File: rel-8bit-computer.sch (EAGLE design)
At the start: 199 parts, among them IC1 74LS04N, IC12 74LS139N, IC2 74LS04N, IC3 74LS04N, IC35 74LS32N, IC37 74LS08N, IC38 74LS08N, IC39 74LS32N, IC4 74LS04N, IC41 74LS08N, IC42 74LS32N, IC44 74LS08N, IC45 74LS32N, IC46 74LS86N, IC47 74LS86N, IC48 74LS32N, IC5 74LS04N, IC50 74LS08N, IC51 74LS08N, IC52 74LS32N, IC54 74LS08N, IC55 74LS32N, IC57 74LS08N, IC58 74LS32N, IC6 74LS04N, IC7 74LS04N, IC8 74LS04N, Q1 BC556, Q2 BS170

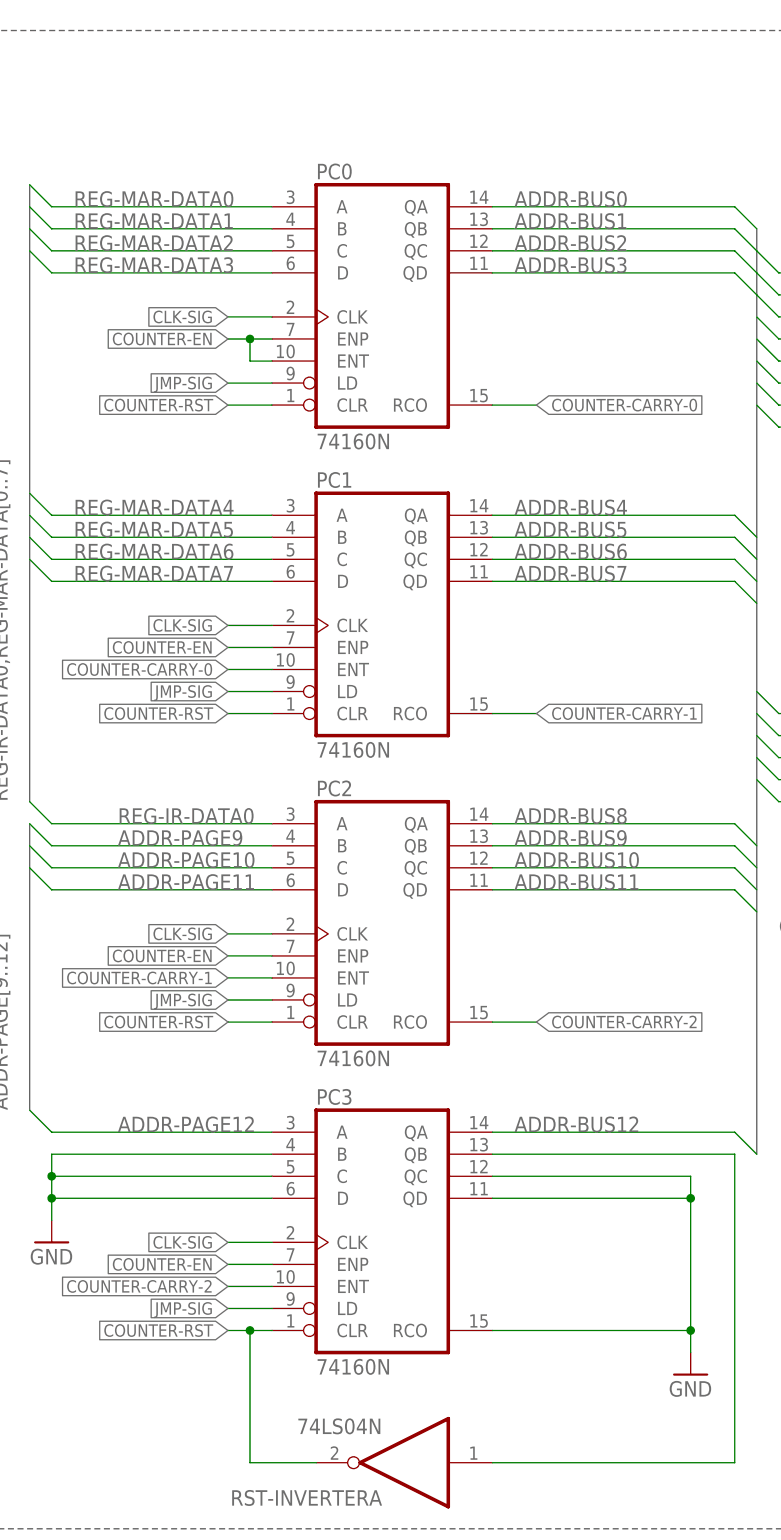
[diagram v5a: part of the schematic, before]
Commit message: Added initial description for PC (program counter) design
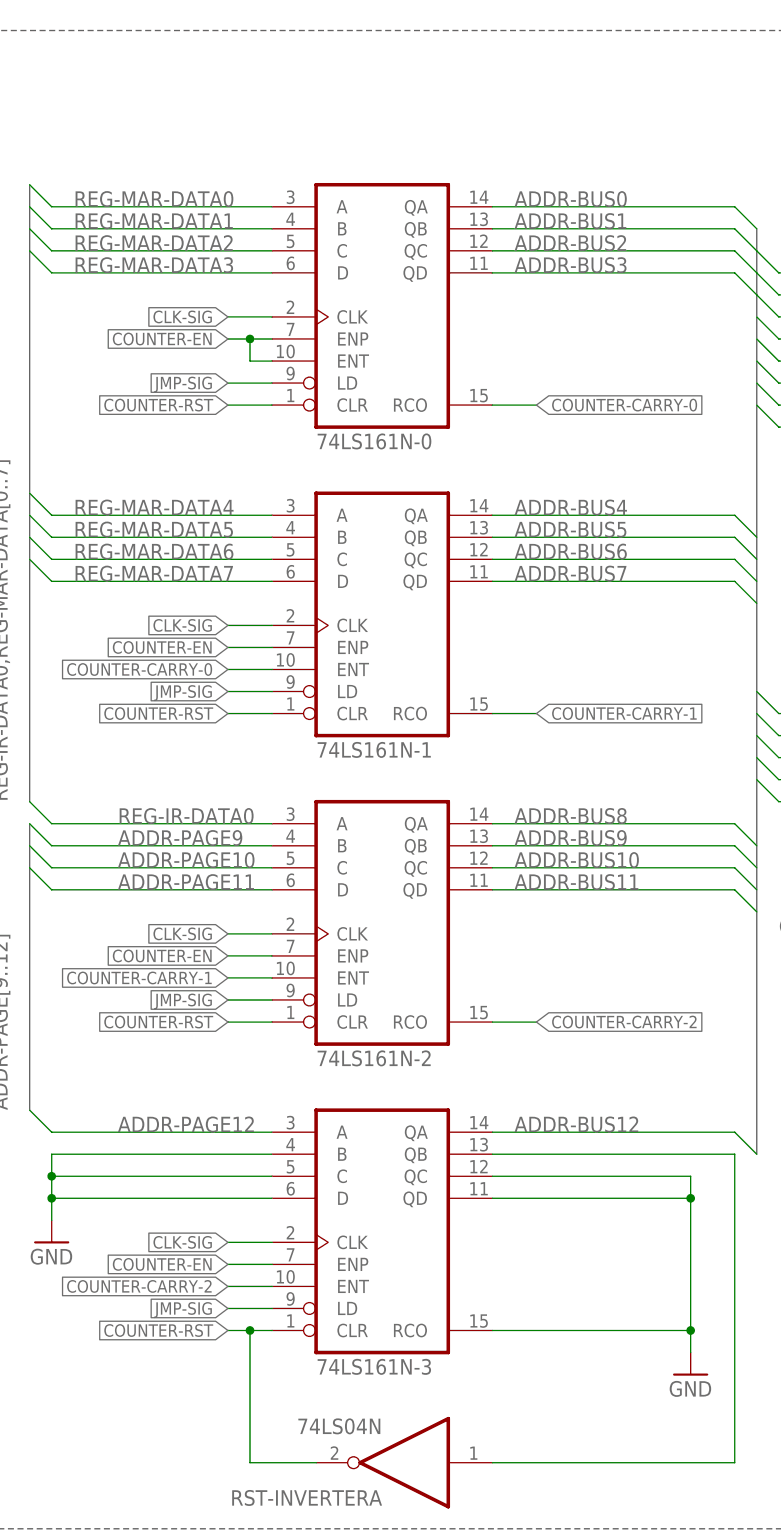
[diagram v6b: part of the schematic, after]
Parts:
- renumbered PC0 to 74LS161N-0, PC1 to 74LS161N-1, PC2 to 74LS161N-2, PC3 to 74LS161N-3

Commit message: Fixed PCH in/out added CS (chip select) reg
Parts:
- added CHIP-SELECT-REG-0: 74LS173N, 74xx-eu:74LS173N
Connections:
- net COUNTER0-OUT renamed PCL-OUT
- net COUNTER1-OUT renamed PCH-OUT
- net MEM-EN-A0 renamed CEN-A0
- net MEM-EN-A1 renamed CEN-A1
- net MEM-EN-A2 renamed CEN-A2
- net MEM-EN-A3 renamed CEN-A3
- net MEM-EN-B0 renamed CEN-B0
- net MEM-EN-B1 renamed CEN-B1
- net MEM-EN-B2 renamed CEN-B2
- net MEM-EN-B3 renamed CEN-B3
- removed net ADDR-BUS10: 74LS161N-2A.QC, ADDR-R/P-SW-2A.3A, PC-BUF-HA.A3
- removed net ADDR-BUS11: 74LS161N-2A.QD, ADDR-R/P-SW-2A.4A, PC-BUF-HA.A4
- removed net ADDR-BUS8: 74LS161N-2A.QA, ADDR-R/P-SW-2A.1A, PC-BUF-HA.A1
- removed net ADDR-BUS9: 74LS161N-2A.QB, ADDR-R/P-SW-2A.2A, PC-BUF-HA.A2
- removed net ADDR-PAGE12: 74LS161N-3A.A, PAGE-ADDR-REG-0A.Q4
- removed net JMP-SIG: 74LS161N-0A.LD, 74LS161N-1A.LD, 74LS161N-2A.LD, 74LS161N-3A.LD
- new net ADDR-EX: 74LS161N-3A.QA
- new net ADDR-PAGE8: ADDR-R/P-SW-2A.1A
- new net CS-EN: CHIP-SELECT-REG-0A.G1, CHIP-SELECT-REG-0A.G2
- new net CS0: CHIP-SELECT-REG-0A.Q1, DEMUX-2X4-0A.A
- new net CS1: CHIP-SELECT-REG-0A.Q2, DEMUX-2X4-0A.B
- new net PCH-IN: 74LS161N-2A.LD, 74LS161N-3A.LD
- new net PCL-IN: 74LS161N-0A.LD, 74LS161N-1A.LD
- net ADDR-BUS12: now also 74LS161N-3A.A, CHIP-SELECT-REG-0A.Q3; no longer 74LS161N-3A.QA, PC-BUF-HA.A5
- net ADDR-BUS4: now also 74LS161N-2A.QA, PC-BUF-HA.A1
- net ADDR-BUS5: now also 74LS161N-2A.QB, PC-BUF-HA.A2
- net ADDR-BUS6: now also 74LS161N-2A.QC, PC-BUF-HA.A3
- net ADDR-BUS7: now also 74LS161N-2A.QD, PC-BUF-HA.A4
- net ADDR-PAGE10: now also ADDR-R/P-SW-2A.3A; no longer 74LS161N-2A.C, PAGE-ADDR-REG-0A.Q2
- net ADDR-PAGE11: now also ADDR-R/P-SW-2A.4A; no longer 74LS161N-2A.D, PAGE-ADDR-REG-0A.Q3
- net ADDR-PAGE9: now also ADDR-R/P-SW-2A.2A; no longer 74LS161N-2A.B, PAGE-ADDR-REG-0A.Q1
- net CLK-SIG: now also CHIP-SELECT-REG-0A.CLK
- net DATA-BUS0: now also 74LS161N-0A.A, CHIP-SELECT-REG-0A.D1; no longer PAGE-ADDR-REG-0A.D1, PC-BUF-HA.B1
- net DATA-BUS1: now also 74LS161N-0A.B, CHIP-SELECT-REG-0A.D2; no longer PAGE-ADDR-REG-0A.D2, PC-BUF-HA.B2
- net DATA-BUS2: now also 74LS161N-0A.C, CHIP-SELECT-REG-0A.D3; no longer PAGE-ADDR-REG-0A.D3, PC-BUF-HA.B3
- net DATA-BUS3: now also 74LS161N-0A.D, CHIP-SELECT-REG-0A.D4; no longer PAGE-ADDR-REG-0A.D4, PC-BUF-HA.B4
- net DATA-BUS4: now also 74LS161N-1A.A, 74LS161N-2A.A, PAGE-ADDR-REG-0A.D1, PAGE-ADDR-REG-0A.Q1, PC-BUF-HA.B1; no longer PC-BUF-HA.B5
- net DATA-BUS5: now also 74LS161N-1A.B, 74LS161N-2A.B, PAGE-ADDR-REG-0A.D2, PAGE-ADDR-REG-0A.Q2, PC-BUF-HA.B2; no longer PC-BUF-HA.B6
- net DATA-BUS6: now also 74LS161N-1A.C, 74LS161N-2A.C, PAGE-ADDR-REG-0A.D3, PAGE-ADDR-REG-0A.Q3, PC-BUF-HA.B3; no longer PC-BUF-HA.B7
- net DATA-BUS7: now also 74LS161N-1A.D, 74LS161N-2A.D, PAGE-ADDR-REG-0A.D4, PAGE-ADDR-REG-0A.Q4, PC-BUF-HA.B4; no longer PC-BUF-HA.B8
- net GND: now also CHIP-SELECT-REG-0A.CLR, CHIP-SELECT-REG-0A.M, CHIP-SELECT-REG-0A.N, CHIP-SELECT-REG-0A.Q4, PC-BUF-HA.A5, PC-BUF-HA.B5, PC-BUF-HA.B6, PC-BUF-HA.B7, PC-BUF-HA.B8
- net REG-IR-DATA0: no longer 74LS161N-2A.A
- net REG-IR-DATA1: no longer DEMUX-2X4-0A.A
- net REG-IR-DATA2: no longer DEMUX-2X4-0A.B
- net REG-MAR-DATA0: no longer 74LS161N-0A.A
- net REG-MAR-DATA1: no longer 74LS161N-0A.B
- net REG-MAR-DATA2: no longer 74LS161N-0A.C
- net REG-MAR-DATA3: no longer 74LS161N-0A.D
- net REG-MAR-DATA4: no longer 74LS161N-1A.A
- net REG-MAR-DATA5: no longer 74LS161N-1A.B
- net REG-MAR-DATA6: no longer 74LS161N-1A.C
- net REG-MAR-DATA7: no longer 74LS161N-1A.D
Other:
- moved on the sheet: DATA-R/P-SW-0, DATA-R/P-SW-1, MEM-BUF, PAGE-ADDR-REG-0, PROG/RUN-DATA-SW

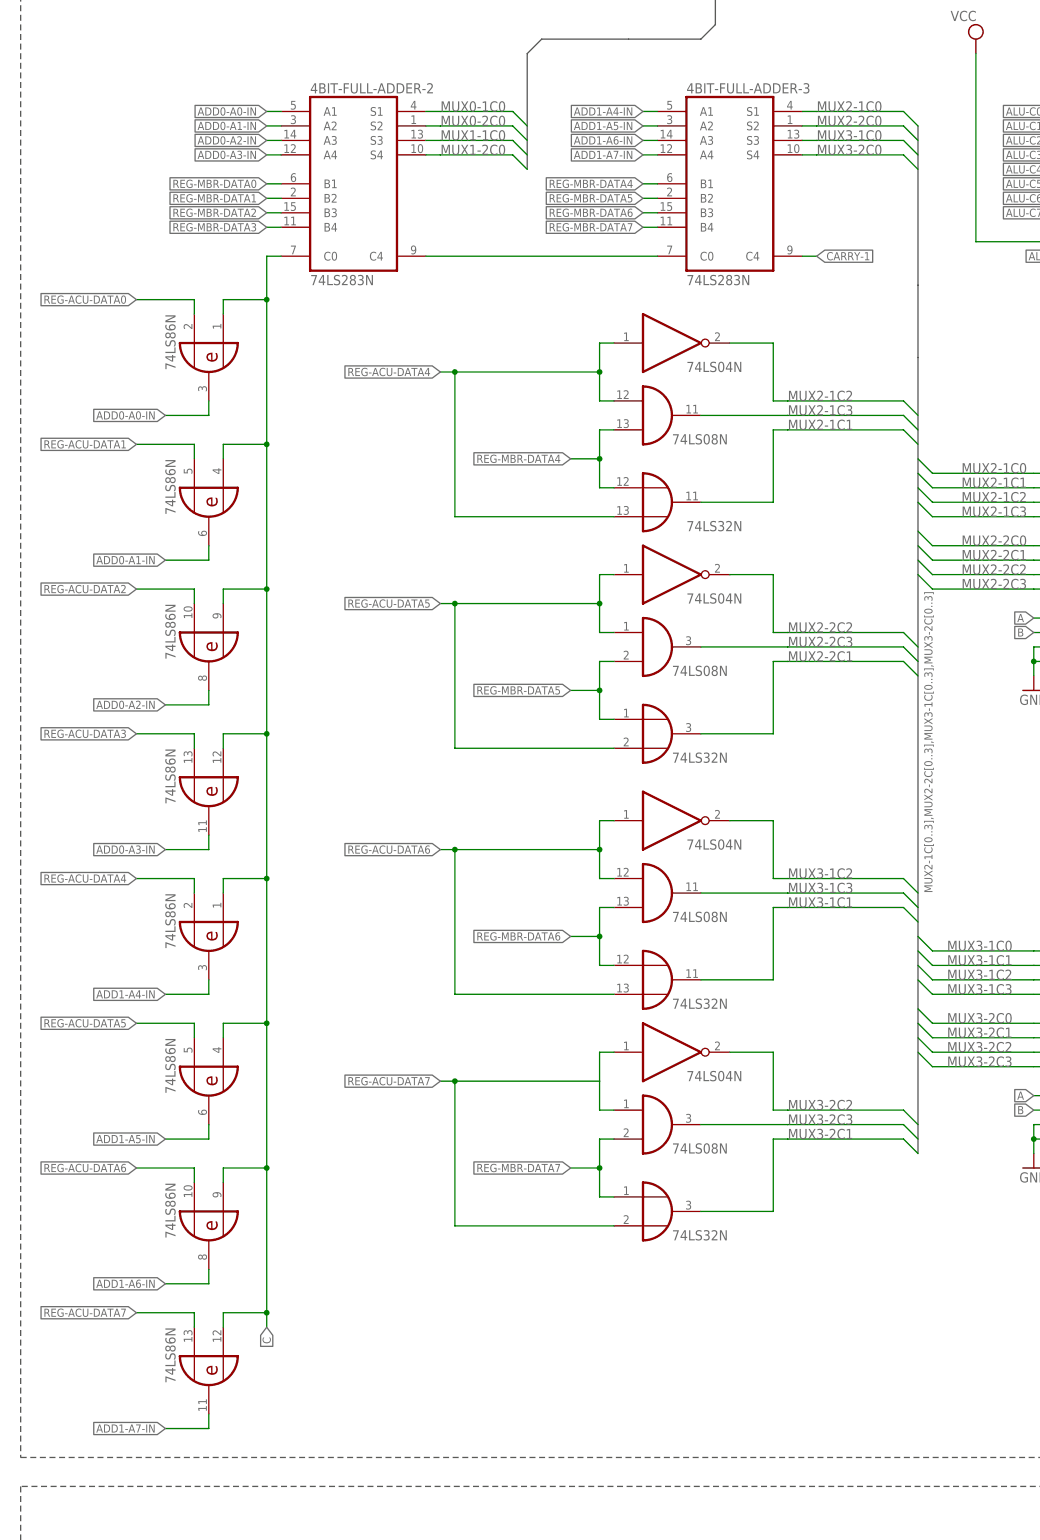
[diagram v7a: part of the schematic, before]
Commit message: Fixed substraction arithmetic
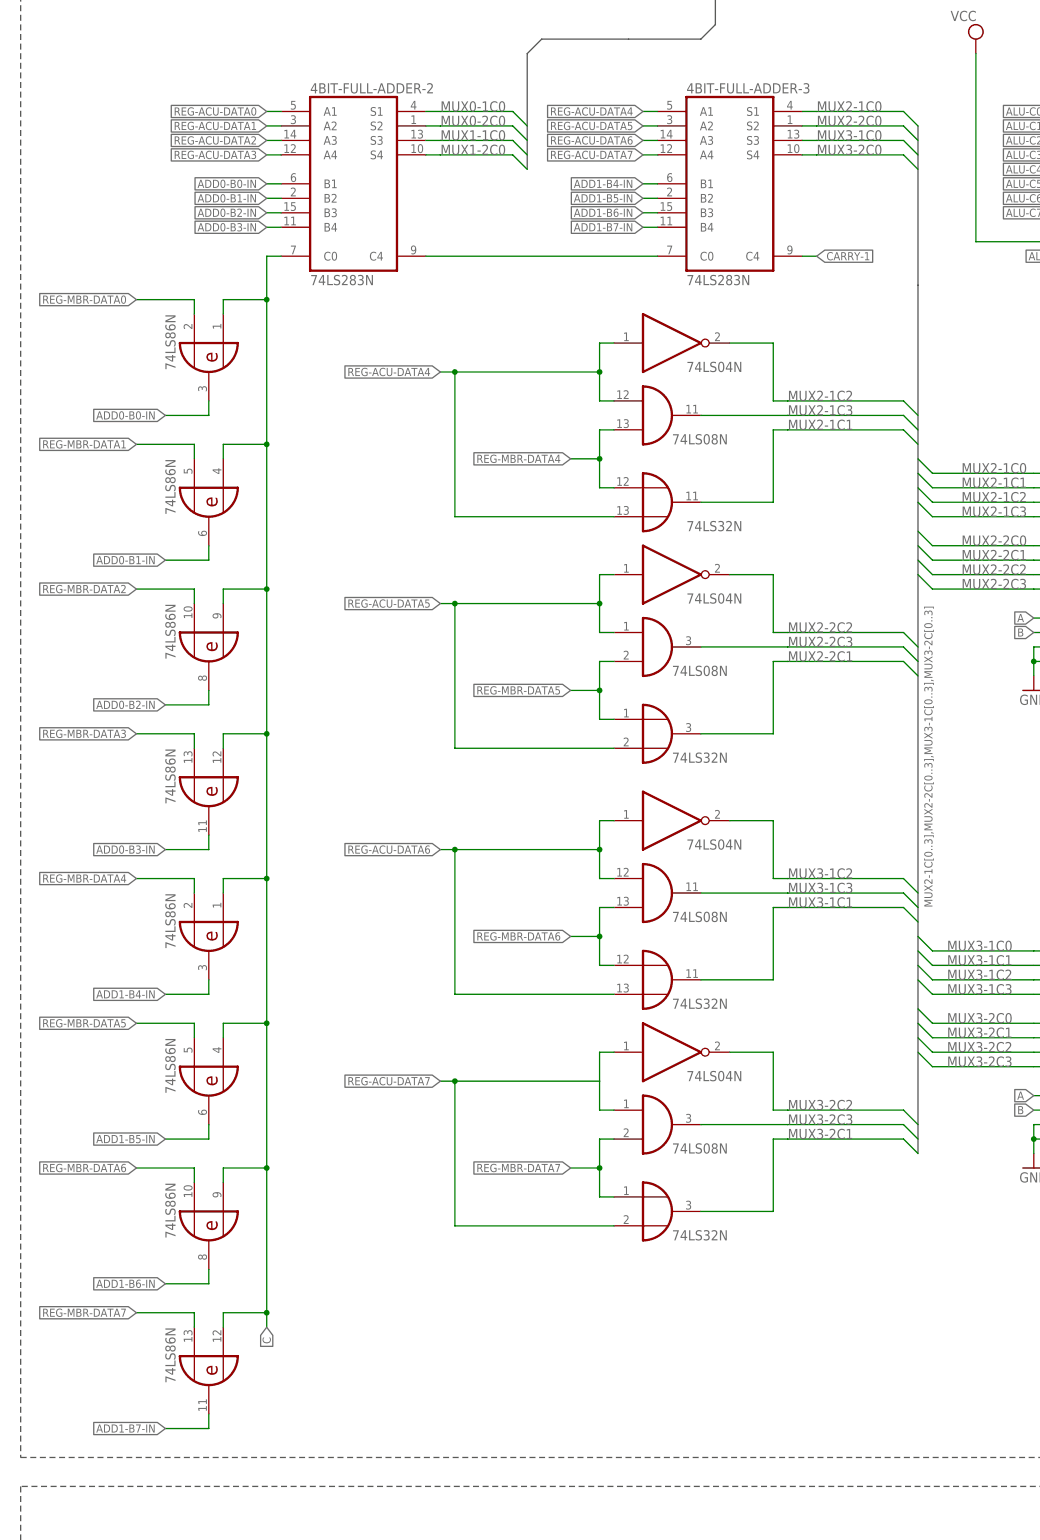
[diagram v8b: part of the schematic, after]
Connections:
- removed net ADD0-A0-IN: 4BIT-FULL-ADDER-2A.A1, IC46A.O
- removed net ADD0-A1-IN: 4BIT-FULL-ADDER-2A.A2, IC46B.O
- removed net ADD0-A2-IN: 4BIT-FULL-ADDER-2A.A3, IC46C.O
- removed net ADD0-A3-IN: 4BIT-FULL-ADDER-2A.A4, IC46D.O
- removed net ADD1-A4-IN: 4BIT-FULL-ADDER-3A.A1, IC47A.O
- removed net ADD1-A5-IN: 4BIT-FULL-ADDER-3A.A2, IC47B.O
- removed net ADD1-A6-IN: 4BIT-FULL-ADDER-3A.A3, IC47C.O
- removed net ADD1-A7-IN: 4BIT-FULL-ADDER-3A.A4, IC47D.O
- new net ADD0-B0-IN: 4BIT-FULL-ADDER-2A.B1, IC46A.O
- new net ADD0-B1-IN: 4BIT-FULL-ADDER-2A.B2, IC46B.O
- new net ADD0-B2-IN: 4BIT-FULL-ADDER-2A.B3, IC46C.O
- new net ADD0-B3-IN: 4BIT-FULL-ADDER-2A.B4, IC46D.O
- new net ADD1-B4-IN: 4BIT-FULL-ADDER-3A.B1, IC47A.O
- new net ADD1-B5-IN: 4BIT-FULL-ADDER-3A.B2, IC47B.O
- new net ADD1-B6-IN: 4BIT-FULL-ADDER-3A.B3, IC47C.O
- new net ADD1-B7-IN: 4BIT-FULL-ADDER-3A.B4, IC47D.O
- net REG-ACU-DATA0: now also 4BIT-FULL-ADDER-2A.A1; no longer IC46A.I1
- net REG-ACU-DATA1: now also 4BIT-FULL-ADDER-2A.A2; no longer IC46B.I1
- net REG-ACU-DATA2: now also 4BIT-FULL-ADDER-2A.A3; no longer IC46C.I1
- net REG-ACU-DATA3: now also 4BIT-FULL-ADDER-2A.A4; no longer IC46D.I1
- net REG-ACU-DATA4: now also 4BIT-FULL-ADDER-3A.A1; no longer IC47A.I1
- net REG-ACU-DATA5: now also 4BIT-FULL-ADDER-3A.A2; no longer IC47B.I1
- net REG-ACU-DATA6: now also 4BIT-FULL-ADDER-3A.A3; no longer IC47C.I1
- net REG-ACU-DATA7: now also 4BIT-FULL-ADDER-3A.A4; no longer IC47D.I1
- net REG-MBR-DATA0: now also IC46A.I1; no longer 4BIT-FULL-ADDER-2A.B1
- net REG-MBR-DATA1: now also IC46B.I1; no longer 4BIT-FULL-ADDER-2A.B2
- net REG-MBR-DATA2: now also IC46C.I1; no longer 4BIT-FULL-ADDER-2A.B3
- net REG-MBR-DATA3: now also IC46D.I1; no longer 4BIT-FULL-ADDER-2A.B4
- net REG-MBR-DATA4: now also IC47A.I1; no longer 4BIT-FULL-ADDER-3A.B1
- net REG-MBR-DATA5: now also IC47B.I1; no longer 4BIT-FULL-ADDER-3A.B2
- net REG-MBR-DATA6: now also IC47C.I1; no longer 4BIT-FULL-ADDER-3A.B3
- net REG-MBR-DATA7: now also IC47D.I1; no longer 4BIT-FULL-ADDER-3A.B4
